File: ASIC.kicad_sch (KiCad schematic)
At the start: 36 parts, among them U10 MCP1824T-1202E/OT, U11 MCP1824T-1202E/OT, U12 MCP1824T-1202E/OT, U8 SN74AVC4T774, U9 MCP1824T-1202E/OT, Y2 50MHz

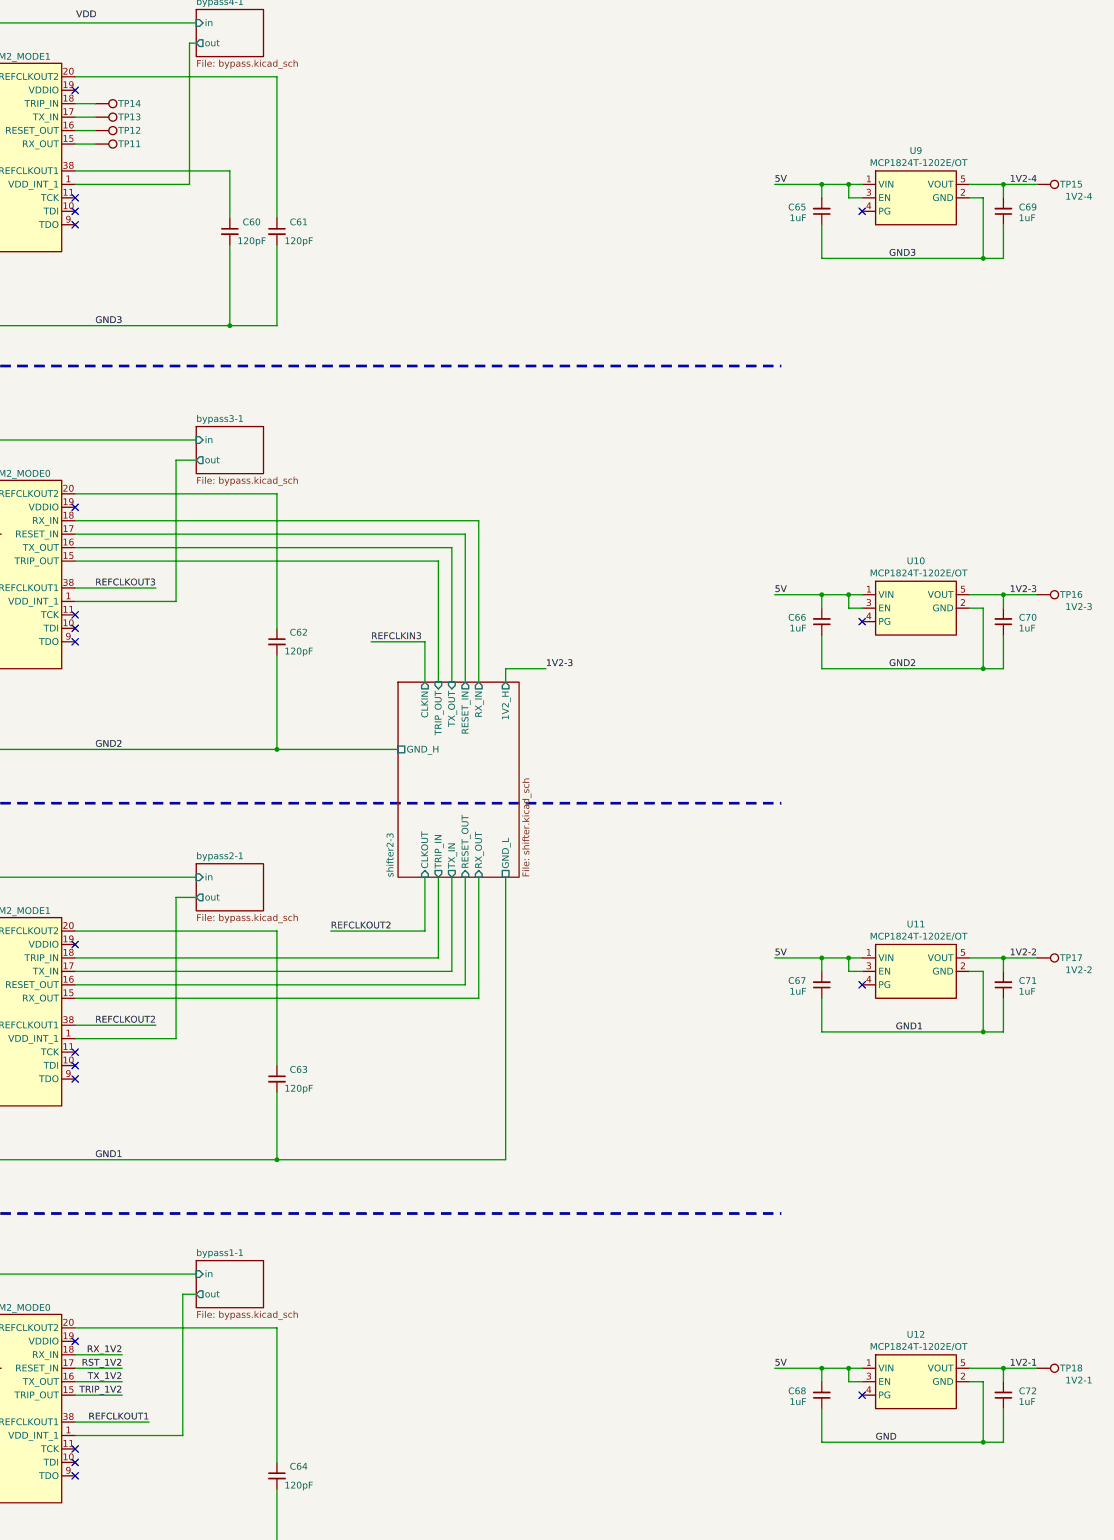
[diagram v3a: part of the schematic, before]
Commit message: switched to TINY LDOs.
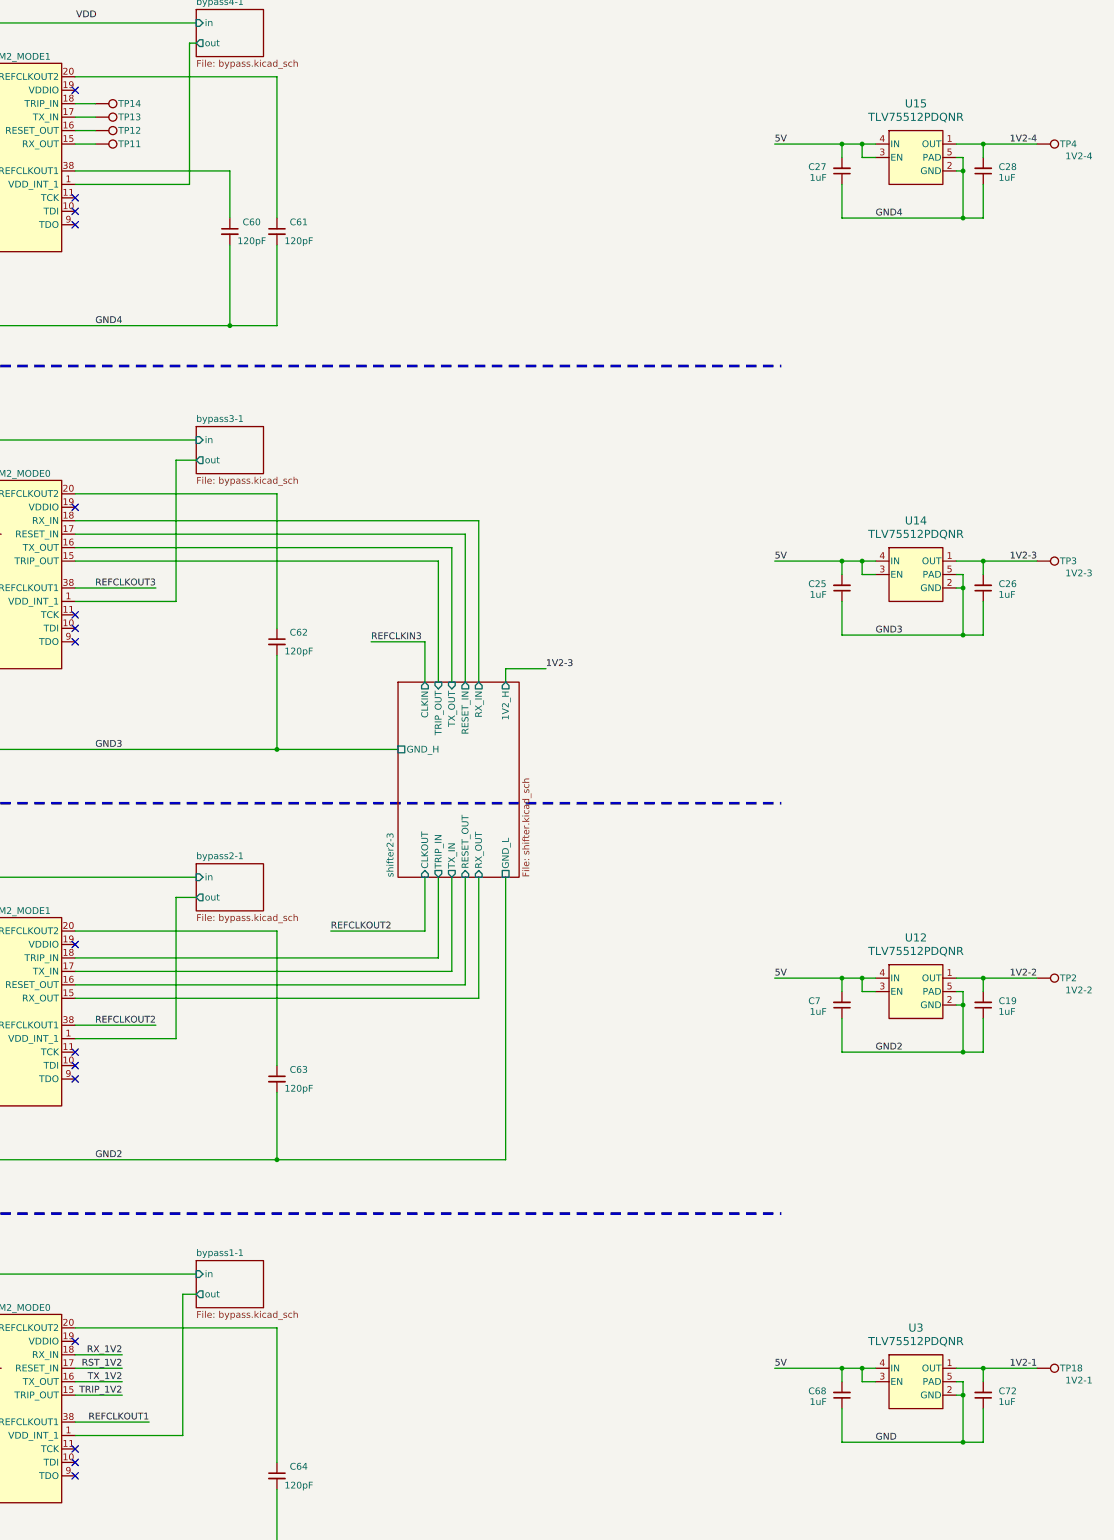
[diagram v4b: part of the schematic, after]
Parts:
- removed C65, C66, C67, C69, C70, C71: 1uF, Capacitor_SMD:C_0402_1005Metric, symbol Device:C_Small
- removed TP15: 1V2-4, bitaxe:TestPoint_Pad_D1.0mm, symbol Connector:TestPoint
- removed TP16: 1V2-3, bitaxe:TestPoint_Pad_D1.0mm, symbol Connector:TestPoint
- removed TP17: 1V2-2, bitaxe:TestPoint_Pad_D1.0mm, symbol Connector:TestPoint
- removed U10, U11, U12, U9: MCP1824T-1202E/OT, Package_TO_SOT_SMD:SOT-23-5, symbol bitaxe:MCP1824
- added C19, C25, C26, C27, C28, C7: 1uF, Capacitor_SMD:C_0402_1005Metric, symbol Device:C_Small
- added TP2: 1V2-2, bitaxe:TestPoint_Pad_D1.0mm, symbol Connector:TestPoint
- added TP3: 1V2-3, bitaxe:TestPoint_Pad_D1.0mm, symbol Connector:TestPoint
- added TP4: 1V2-4, bitaxe:TestPoint_Pad_D1.0mm, symbol Connector:TestPoint
- added U12, U14, U15, U3: TLV75512PDQNR, bitaxe:DQN0004A, symbol bitaxe:TLV75512PDQNR
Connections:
- net GND1 is gone; now on net GND2: A1.2 (VDD), A1.3 (VDD), A1.4 (VDD), A1.41 (VDD), A1.42 (VDD), A1.49 (VDD), A1.5 (VDD), A1.50 (VDD), A1.51 (VDD), A1.52 (VDD), A1.59 (VDD), A1.6 (VDD), A1.60 (VDD), A1.7 (VDD), A1.8 (VDD), A2.14 (VSS), A2.21 (VSS), A2.22 (VSS), A2.23 (VSS), A2.24 (VSS), A2.25 (VSS), A2.26 (VSS), A2.27 (VSS), A2.28 (VSS), A2.35 (VSS), A2.43 (VSS), A2.44 (VSS), A2.45 (VSS), A2.46 (VSS), A2.47 (VSS), A2.48 (VSS), A2.53 (VSS), A2.54 (VSS), A2.55 (VSS), A2.56 (VSS), A2.57 (VSS), A2.58 (VSS), C63.2
- net 1V2-1: now also U3.1 (OUT)
- net 1V2-2: now also C19.2, TP2.1, U12.1 (OUT)
- net 1V2-3: now also C26.2, TP3.1, U14.1 (OUT)
- net 1V2-4: now also C28.2, TP4.1, U15.1 (OUT)
- net 5V: now also C25.2, C27.2, C7.2, U12.3 (EN), U12.4 (IN), U14.3 (EN), U14.4 (IN), U15.3 (EN), U15.4 (IN), U3.3 (EN), U3.4 (IN)
- net GND: now also U3.2 (GND), U3.5 (PAD)
- net GND2: now also C19.1, C7.1, U12.2 (GND), U12.5 (PAD); no longer A2.2 (VDD), A2.3 (VDD), A2.4 (VDD), A2.41 (VDD), A2.42 (VDD), A2.49 (VDD), A2.5 (VDD), A2.50 (VDD), A2.51 (VDD), A2.52 (VDD), A2.59 (VDD), A2.6 (VDD), A2.60 (VDD), A2.7 (VDD), A2.8 (VDD), A3.14 (VSS), A3.21 (VSS), A3.22 (VSS), A3.23 (VSS), A3.24 (VSS), A3.25 (VSS), A3.26 (VSS), A3.27 (VSS), A3.28 (VSS), A3.35 (VSS), A3.43 (VSS), A3.44 (VSS), A3.45 (VSS), A3.46 (VSS), A3.47 (VSS), A3.48 (VSS), A3.53 (VSS), A3.54 (VSS), A3.55 (VSS), A3.56 (VSS), A3.57 (VSS), A3.58 (VSS), C62.2
- net GND3: now also A2.2 (VDD), A2.3 (VDD), A2.4 (VDD), A2.41 (VDD), A2.42 (VDD), A2.49 (VDD), A2.5 (VDD), A2.50 (VDD), A2.51 (VDD), A2.52 (VDD), A2.59 (VDD), A2.6 (VDD), A2.60 (VDD), A2.7 (VDD), A2.8 (VDD), A3.14 (VSS), A3.21 (VSS), A3.22 (VSS), A3.23 (VSS), A3.24 (VSS), A3.25 (VSS), A3.26 (VSS), A3.27 (VSS), A3.28 (VSS), A3.35 (VSS), A3.43 (VSS), A3.44 (VSS), A3.45 (VSS), A3.46 (VSS), A3.47 (VSS), A3.48 (VSS), A3.53 (VSS), A3.54 (VSS), A3.55 (VSS), A3.56 (VSS), A3.57 (VSS), A3.58 (VSS), C62.2, C25.1, C26.1, U14.2 (GND), U14.5 (PAD); no longer A3.2 (VDD), A3.3 (VDD), A3.4 (VDD), A3.41 (VDD), A3.42 (VDD), A3.49 (VDD), A3.5 (VDD), A3.50 (VDD), A3.51 (VDD), A3.52 (VDD), A3.59 (VDD), A3.6 (VDD), A3.60 (VDD), A3.7 (VDD), A3.8 (VDD), A4.14 (VSS), A4.21 (VSS), A4.22 (VSS), A4.23 (VSS), A4.24 (VSS), A4.25 (VSS), A4.26 (VSS), A4.27 (VSS), A4.28 (VSS), A4.35 (VSS), A4.43 (VSS), A4.44 (VSS), A4.45 (VSS), A4.46 (VSS), A4.47 (VSS), A4.48 (VSS), A4.53 (VSS), A4.54 (VSS), A4.55 (VSS), A4.56 (VSS), A4.57 (VSS), A4.58 (VSS), C60.2, C61.2
- new net GND4: A3.2 (VDD), A3.3 (VDD), A3.4 (VDD), A3.41 (VDD), A3.42 (VDD), A3.49 (VDD), A3.5 (VDD), A3.50 (VDD), A3.51 (VDD), A3.52 (VDD), A3.59 (VDD), A3.6 (VDD), A3.60 (VDD), A3.7 (VDD), A3.8 (VDD), A4.14 (VSS), A4.21 (VSS), A4.22 (VSS), A4.23 (VSS), A4.24 (VSS), A4.25 (VSS), A4.26 (VSS), A4.27 (VSS), A4.28 (VSS), A4.35 (VSS), A4.43 (VSS), A4.44 (VSS), A4.45 (VSS), A4.46 (VSS), A4.47 (VSS), A4.48 (VSS), A4.53 (VSS), A4.54 (VSS), A4.55 (VSS), A4.56 (VSS), A4.57 (VSS), A4.58 (VSS), C27.1, C28.1, C60.2, C61.2, U15.2 (GND), U15.5 (PAD)
- no-connect marks 30 -> 26
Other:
- moved on the sheet: C68, C72

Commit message: Added RP Pico W2 to schematic. Fixed Domain 1-2 level shifter pins. Added test points
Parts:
- added TP17, TP20, TP21, TP22, TP6: SDA, bitaxe:TestPoint_Pad_D1.0mm, symbol Connector:TestPoint
- added TP28, TP43: TTI, bitaxe:TestPoint_Pad_1.0x0.4mm, symbol Connector:TestPoint
- added TP29, TP44: TXI, bitaxe:TestPoint_Pad_1.0x0.4mm, symbol Connector:TestPoint
- added TP30, TP39, TP45: RSTO, bitaxe:TestPoint_Pad_1.0x0.4mm, symbol Connector:TestPoint
- added TP31, TP38, TP46: RXO, bitaxe:TestPoint_Pad_1.0x0.4mm, symbol Connector:TestPoint
- added TP32, TP51, TP55: RSTI, bitaxe:TestPoint_Pad_1.0x0.4mm, symbol Connector:TestPoint
- added TP33, TP40, TP50, TP54: TXO, bitaxe:TestPoint_Pad_1.0x0.4mm, symbol Connector:TestPoint
- added TP34, TP41, TP49, TP53: TTO, bitaxe:TestPoint_Pad_1.0x0.4mm, symbol Connector:TestPoint
- added TP35, TP48, TP57: CLKI, bitaxe:TestPoint_Pad_1.0x0.4mm, symbol Connector:TestPoint
- added TP36, TP52, TP56: RXI, bitaxe:TestPoint_Pad_1.0x0.4mm, symbol Connector:TestPoint
- added TP37, TP42, TP47: CLKO, bitaxe:TestPoint_Pad_1.0x0.4mm, symbol Connector:TestPoint
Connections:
- net GND: now also TP22.1
- net REFCLKIN2: now also TP35.1
- net REFCLKIN3: now also TP57.1
- net REFCLKIN4: now also TP48.1
- net REFCLKOUT1: now also TP37.1
- net REFCLKOUT2: now also TP42.1
- net REFCLKOUT3: now also TP47.1
- net RST_1V2: now also TP6.1
- net RX_1V2: now also TP20.1
- net TRIP_1V2: now also TP21.1
- net TX_1V2: now also TP17.1
- net shifter1-2/RESET_IN: now also A2.33 (RESET_IN), TP32.1; no longer A2.32 (TX_OUT)
- net shifter1-2/RESET_OUT: now also A1.32 (RESET_OUT), TP30.1; no longer A1.33 (TX_IN)
- net shifter1-2/RX_IN: now also A2.34 (RX_IN), TP36.1; no longer A2.31 (TRIP_OUT)
- net shifter1-2/RX_OUT: now also A1.31 (RX_OUT), TP31.1; no longer A1.34 (TRIP_IN)
- net shifter1-2/TRIP_IN: now also A1.34 (TRIP_IN), TP28.1; no longer A1.31 (RX_OUT)
- net shifter1-2/TRIP_OUT: now also A2.31 (TRIP_OUT), TP34.1; no longer A2.34 (RX_IN)
- net shifter1-2/TX_IN: now also A1.33 (TX_IN), TP29.1; no longer A1.32 (RESET_OUT)
- net shifter1-2/TX_OUT: now also A2.32 (TX_OUT), TP33.1; no longer A2.33 (RESET_IN)
- net shifter2-3/RESET_IN: now also TP55.1
- net shifter2-3/RESET_OUT: now also TP39.1
- net shifter2-3/RX_IN: now also TP56.1
- net shifter2-3/RX_OUT: now also TP38.1
- net shifter2-3/TRIP_IN: now also TP41.1
- net shifter2-3/TRIP_OUT: now also TP53.1
- net shifter2-3/TX_IN: now also TP40.1
- net shifter2-3/TX_OUT: now also TP54.1
- net shifter3-4/RESET_IN: now also TP51.1
- net shifter3-4/RESET_OUT: now also TP45.1
- net shifter3-4/RX_IN: now also TP52.1
- net shifter3-4/RX_OUT: now also TP46.1
- net shifter3-4/TRIP_IN: now also TP43.1
- net shifter3-4/TRIP_OUT: now also TP49.1
- net shifter3-4/TX_IN: now also TP44.1
- net shifter3-4/TX_OUT: now also TP50.1
- net 5V renamed 5V_SWITCH
- net GND2 renamed DOMAIN1
- net GND3 renamed DOMAIN2
- net GND4 renamed DOMAIN3
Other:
- note added: "DOMAIN 1"
- note added: "DOMAIN 2"
- note added: "DOMAIN 3"
- note added: "DOMAIN 4"
- moved on the sheet: C57

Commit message: switched to THT RPi Pico 2W style. Made 8mm taller.
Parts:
- TP14: value TRP -> TT
- TP17: value SDA -> TX
- TP20: value SDA -> RX
- TP21: value SDA -> TT
- TP22: value SDA -> GND
- TP6: value SDA -> RST
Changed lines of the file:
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@@
 			)
 		)
-		(property "Value" "TRP"
+		(property "Value" "TT"
 			(at 314.198 79.756 90)
 			(effects
@@
 			)
 		)
-		(property "Value" "SDA"
+		(property "Value" "TX"
 			(at 83.185 76.2001 90)
 			(effects
@@
 			)
 		)
-		(property "Value" "SDA"
+		(property "Value" "TT"
 			(at 83.185 81.2801 90)
 			(effects
@@
 			)
 		)
-		(property "Value" "SDA"
+		(property "Value" "GND"
 			(at 70.485 85.0901 90)
 			(effects
@@
 			)
 		)
-		(property "Value" "SDA"
+		(property "Value" "RX"
 			(at 83.185 78.7401 90)
 			(effects
@@
 			)
 		)
-		(property "Value" "SDA"
+		(property "Value" "RST"
 			(at 83.185 73.6601 90)
 			(effects

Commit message: lots of routing
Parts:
- TP11: value RX -> TTI; footprint bitaxe:TestPoint_Pad_D1.0mm -> bitaxe:TestPoint_Pad_1.0x0.4mm
- TP12: value RST -> TXI; footprint bitaxe:TestPoint_Pad_D1.0mm -> bitaxe:TestPoint_Pad_1.0x0.4mm
- TP13: value TX -> RSTI; footprint bitaxe:TestPoint_Pad_D1.0mm -> bitaxe:TestPoint_Pad_1.0x0.4mm
- TP14: value TT -> RXO; footprint bitaxe:TestPoint_Pad_D1.0mm -> bitaxe:TestPoint_Pad_1.0x0.4mm
- TP17: value TX -> TXO; footprint bitaxe:TestPoint_Pad_D1.0mm -> bitaxe:TestPoint_Pad_1.0x0.4mm
- TP20: value RX -> RXI; footprint bitaxe:TestPoint_Pad_D1.0mm -> bitaxe:TestPoint_Pad_1.0x0.4mm
- TP21: value TT -> TTO; footprint bitaxe:TestPoint_Pad_D1.0mm -> bitaxe:TestPoint_Pad_1.0x0.4mm
- TP22: footprint bitaxe:TestPoint_Pad_D1.0mm -> bitaxe:TestPoint_Pad_1.0x0.4mm
- TP6: value RST -> RSTI; footprint bitaxe:TestPoint_Pad_D1.0mm -> bitaxe:TestPoint_Pad_1.0x0.4mm
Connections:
- net at TP14.1: now also A4.15 (RX_OUT); no longer A4.18 (TRIP_IN)
- net at TP11.1: now also A4.18 (TRIP_IN); no longer A4.15 (RX_OUT)
- net at A4.16 (RESET_OUT): now also TP13.1; no longer TP12.1
- net at A4.17 (TX_IN): now also TP12.1; no longer TP13.1

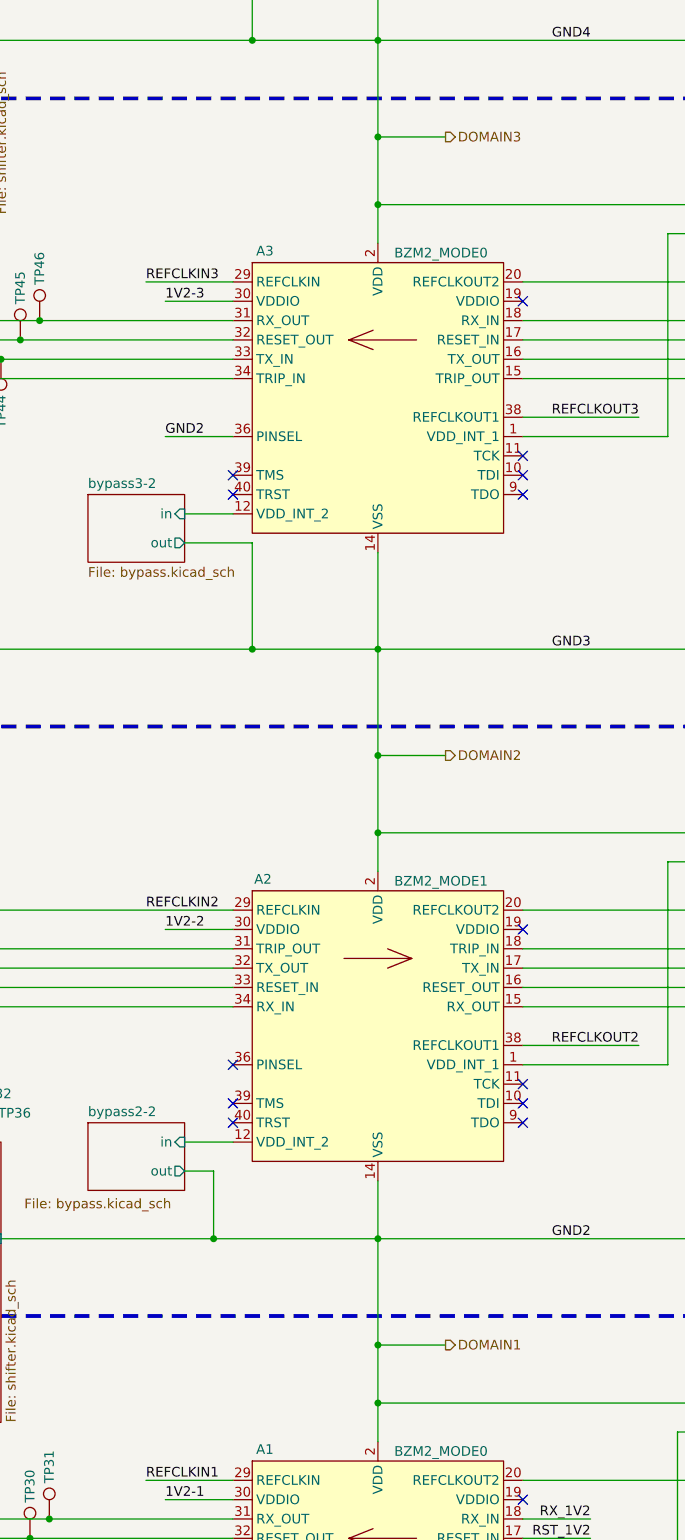
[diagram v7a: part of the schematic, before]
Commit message: routing done, needs DRC and cleanup
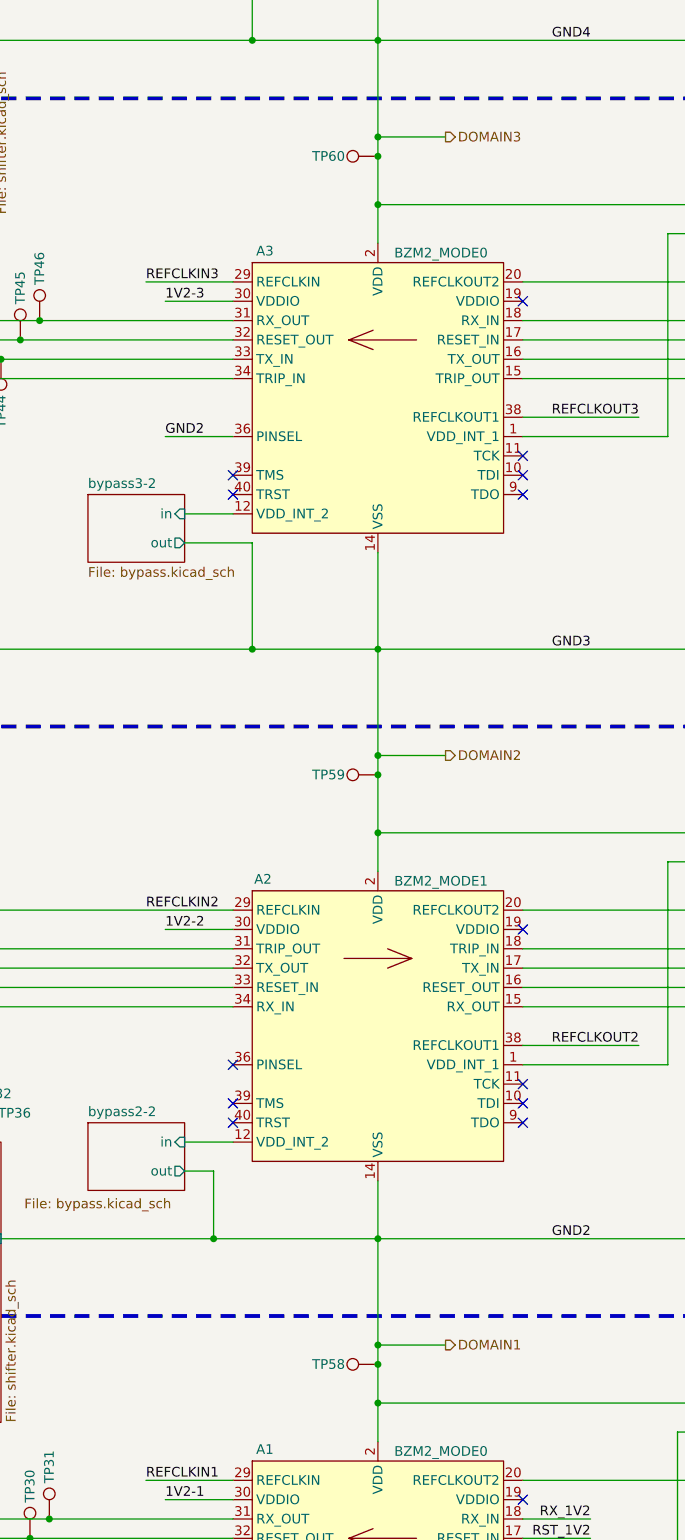
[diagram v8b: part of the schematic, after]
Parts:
- added TP58: D1, bitaxe:TestPoint_Pad_D1.0mm, symbol Connector:TestPoint
- added TP59: D2, bitaxe:TestPoint_Pad_D1.0mm, symbol Connector:TestPoint
- added TP60: D3, bitaxe:TestPoint_Pad_D1.0mm, symbol Connector:TestPoint
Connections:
- net DOMAIN1: now also TP58.1
- net DOMAIN2: now also TP59.1
- net DOMAIN3: now also TP60.1
